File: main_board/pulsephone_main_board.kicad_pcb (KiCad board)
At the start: 2 copper layers, 70.5 x 128.5 mm, 32 parts, among them J1 USB_C_Receptacle_USB2.0_14P, J3 Conn_2Rows-35Pins_MountingPin, J4 Conn_2Rows-35Pins_MountingPin, J5 Conn_2Rows-35Pins_MountingPin, U1 XL1509-3.3, U2 PCM5102APWR, U4 TPS61202DRC, U5 TP4056-42-ESOP8

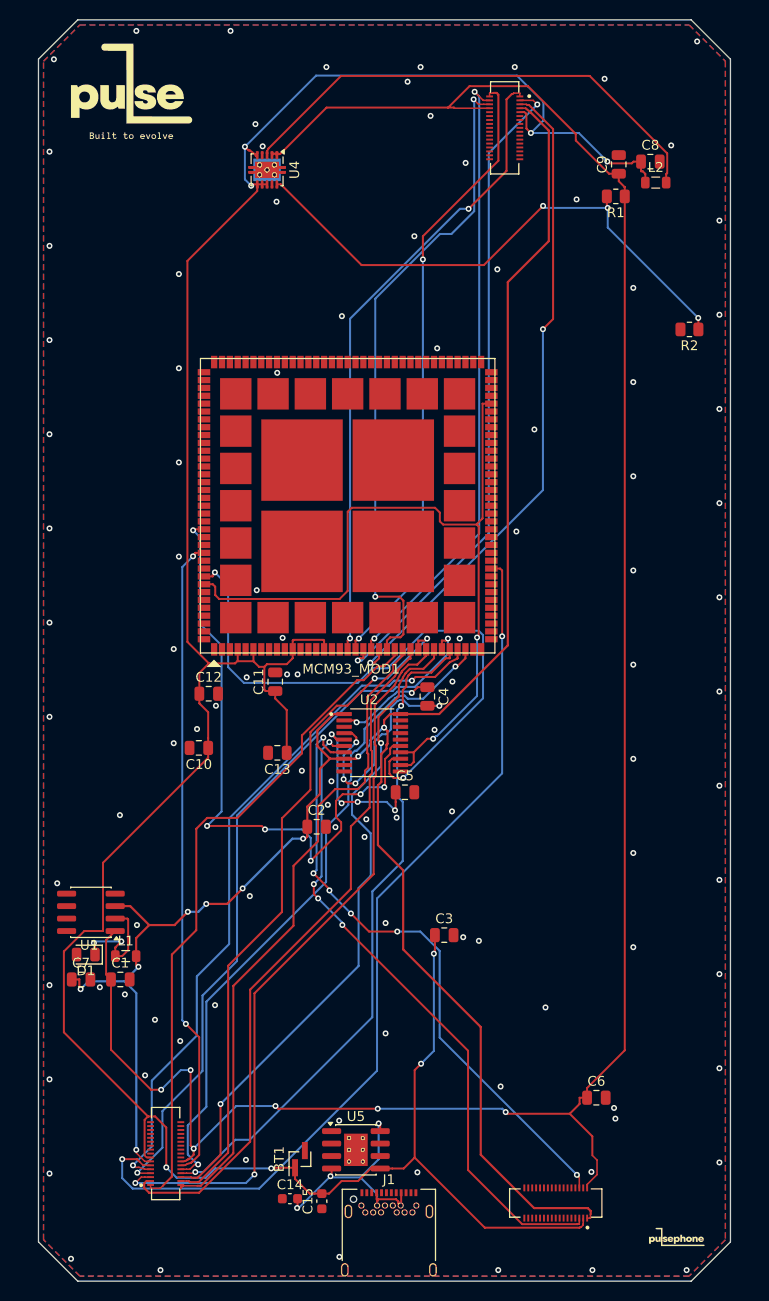
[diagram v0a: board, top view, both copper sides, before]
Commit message: pcb: update board layout and routing
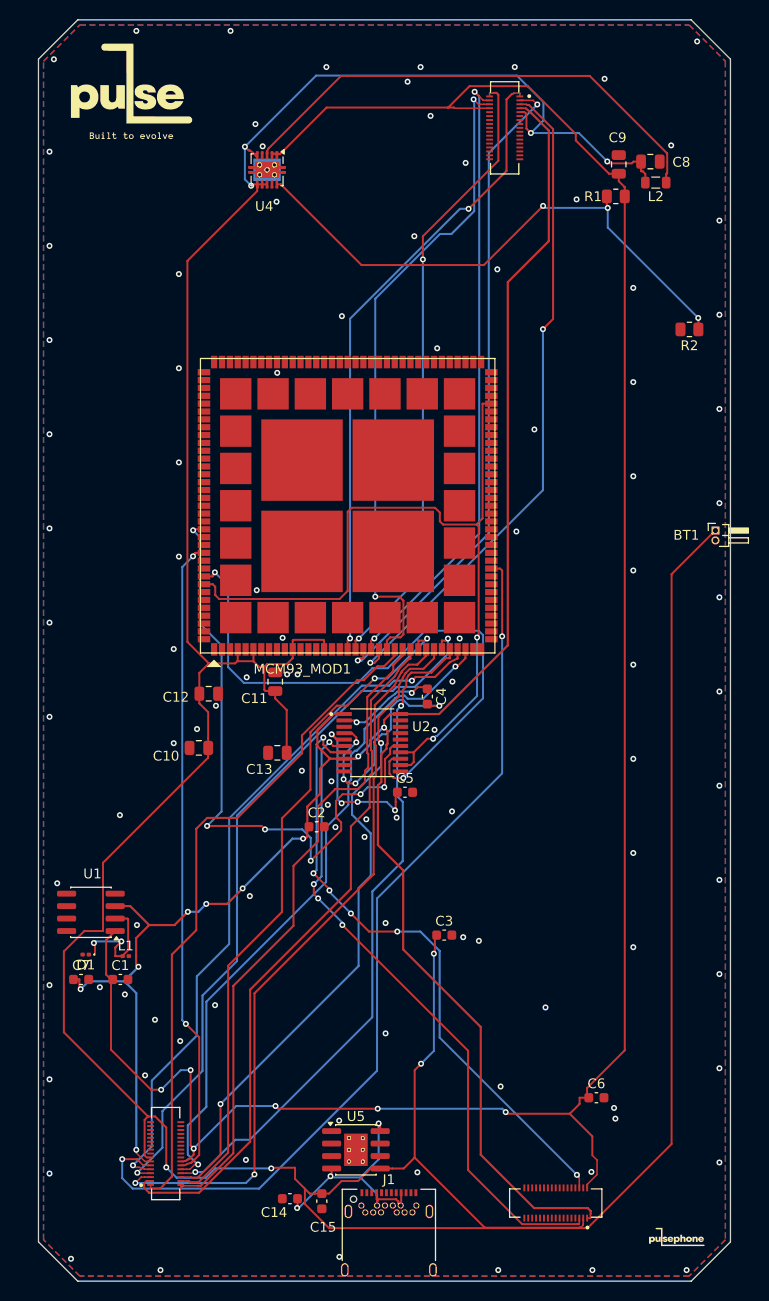
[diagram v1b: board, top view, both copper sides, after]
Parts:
- BT1: footprint Connector_PinHeader_1.00mm:PinHeader_1x02_P1.00mm_Vertical_SMD_Pin1Left -> Connector_PinHeader_1.00mm:PinHeader_1x02_P1.00mm_Horizontal
- C1, C4, C5, C7: footprint Capacitor_SMD:C_0805_2012Metric -> Capacitor_SMD:C_0603_1608Metric
- C2, C3, C6: value 20uF -> 10uF; footprint Capacitor_SMD:C_0805_2012Metric -> Capacitor_SMD:C_0603_1608Metric
- D1: footprint Diode_SMD:D_0805_2012Metric -> Diode_SMD:D_0201_0603Metric
- L1: footprint Inductor_SMD:L_0805_2012Metric -> Inductor_SMD:L_0201_0603Metric
- moved BT1 76.8 mm to (170.0, 78.0), turned to 0 degrees
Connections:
- C1 pad 1: +5V -> +3.7VBAT
- J5 pad 5: Net-(J5-Pin_5) -> unconnected-(J5-Pin_5-Pad5)
- J5 pad 6: Net-(J5-Pin_6) -> unconnected-(J5-Pin_6-Pad6)
- J5 pad 8: unconnected-(J5-Pin_8-Pad8) -> Net-(J5-Pin_8)
- J5 pad 9: unconnected-(J5-Pin_9-Pad9) -> Net-(J5-Pin_9)
- MCM93_MOD1 pad 11: +3.7VBAT -> +5V
- MCM93_MOD1 pad 133: /AUDIO_DATA_OUT -> /SAI_MASTERCLOCK
- MCM93_MOD1 pad 15: +3.7VBAT -> +5V
- MCM93_MOD1 pad 4: +3.7VBAT -> +5V
- MCM93_MOD1 pad 6: +3.7VBAT -> +5V
- U1 pad 1: +5V -> +3.7VBAT
- U1 pad 4: unconnected-(U1-~{EN}-Pad4) -> +3.7VBAT
- U2 pad 12: /AUDIO_DATA_OUT -> /SAI_MASTERCLOCK
- U2 pad 6: Net-(J5-Pin_5) -> Net-(J5-Pin_8)
- U2 pad 7: Net-(J5-Pin_6) -> Net-(J5-Pin_9)
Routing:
- net (no net): track 0.00 -> 130.4 mm, vias 0 -> 10
- net +3.7VBAT: track 287.0 -> 394.8 mm
- net Net-(J5-Pin_5): track 66.7 -> 0.00 mm, vias 4 -> 0
- net Net-(J5-Pin_6): track 63.8 -> 0.00 mm, vias 6 -> 0

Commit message: Redo PCB Routing, and added extra features
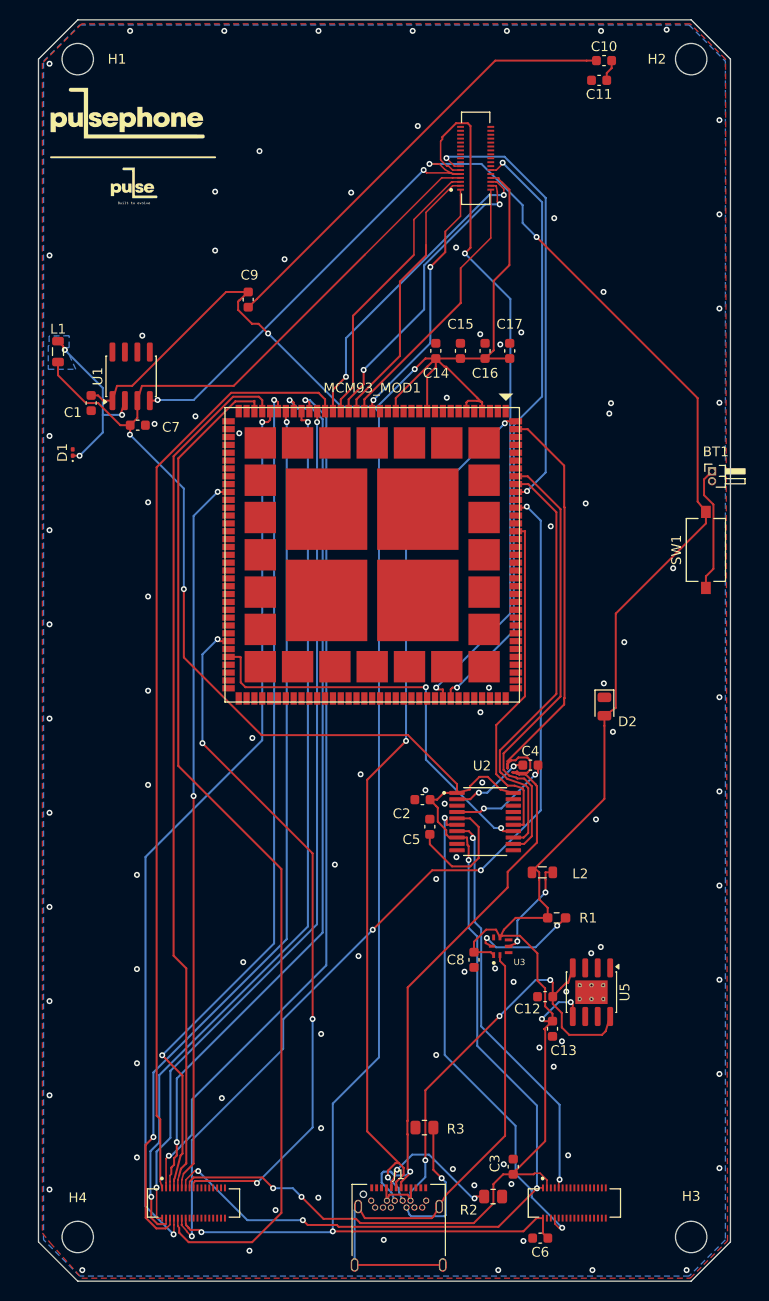
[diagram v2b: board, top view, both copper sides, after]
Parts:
- removed the G*** at (166.0, 150.0)
- removed U4: TPS61202DRC, Package_SON:Texas_S-PVSON-N10_ThermalVias
- removed nul: nul, LOGO
- added C16: 22uF, Capacitor_SMD:C_0603_1608Metric, F.Cu at (146.5, 59.7)
- added C17: 22uF, Capacitor_SMD:C_0603_1608Metric, F.Cu at (149.0, 59.7)
- added D2: LED, LED_SMD:LED_0805_2012Metric, F.Cu at (158.7, 96.0)
- added G***: LOGO, LOGO, F.Cu at (110.8, 43.0)
- added G***: LOGO, LOGO, F.Cu at (110.0, 35.5)
- added H1: MountingHole, MountingHole:MountingHole_3.2mm_M3, F.Cu at (105.0, 30.0)
- added H2: MountingHole, MountingHole:MountingHole_3.2mm_M3, F.Cu at (167.5, 30.0)
- added H3: MountingHole, MountingHole:MountingHole_3.2mm_M3, F.Cu at (167.5, 150.0)
- added H4: MountingHole, MountingHole:MountingHole_3.2mm_M3, F.Cu at (105.0, 150.0)
- added R3: 5.1 kΩ, Resistor_SMD:R_0805_2012Metric, F.Cu at (140.3, 138.9)
- added SW1: SW_DPST_x2, Button_Switch_SMD:SW_Tactile_SPST_NO_Straight_CK_PTS636Sx25SMTRLFS, F.Cu at (169.0, 80.0)
- added U3: ~, MIC2877-5.0YFT-TR:VREG_MIC2877-AYFT-TR, F.Cu at (148.1, 120.4)
- C10, C11, C8, C9: value 20uF -> 22uF; footprint Capacitor_SMD:C_0805_2012Metric -> Capacitor_SMD:C_0603_1608Metric
- C12, C13: value 20uF -> 10uF; footprint Capacitor_SMD:C_0805_2012Metric -> Capacitor_SMD:C_0603_1608Metric
- C14, C15: value 10uF -> 22uF
- L1: footprint Inductor_SMD:L_0201_0603Metric -> Inductor_SMD:L_0805_2012Metric
- L2: value 2.2uh -> 1uH
- R1: value 9Kohm -> 1Mega Ohm; footprint Resistor_SMD:R_0805_2012Metric -> Resistor_SMD:R_0603_1608Metric_Pad0.98x0.95mm_HandSolder
- R2: value 1Kohm -> 5.1 kΩ
- moved R2 90.6 mm to (147.3, 145.9), turned to 0 degrees
- moved C15 87.8 mm to (144.0, 59.7)
- moved C14 87.6 mm to (141.5, 59.7), turned to 90 degrees
- moved C8 83.3 mm to (145.4, 121.8), turned to -90 degrees
- moved C10 81.3 mm to (158.6, 30.1), turned to 0 degrees
- moved R1 73.8 mm to (153.8, 117.5)
- moved L2 71.2 mm to (152.3, 112.9)
- moved C11 69.6 mm to (158.1, 32.2), turned to 180 degrees
- moved L1 62.0 mm to (103.0, 59.8), turned to -90 degrees
- moved C1 58.8 mm to (106.4, 65.0), turned to -90 degrees
- moved C7 56.8 mm to (111.1, 67.3)
- moved U1 54.8 mm to (110.4, 62.3), turned to 90 degrees
- moved D1 51.2 mm to (104.5, 70.1), turned to 90 degrees
- moved C12 46.1 mm to (152.6, 125.5)
- moved C9 40.2 mm to (122.4, 54.5), turned to -90 degrees
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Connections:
- BT1 pad 1: +3.7VBAT -> Net-(BT1-+)
- C1 pad 1: +3.7VBAT -> +5V
- C10 pad 1: +3.7VBAT -> Net-(C10-Pad1)
- C10 pad 2: GND -> Net-(C10-Pad2)
- C11 pad 1: +3.7VBAT -> Net-(C10-Pad2)
- C12 pad 1: +3.7VBAT -> GND
- C12 pad 2: GND -> Net-(U5-CE)
- C13 pad 1: +3.7VBAT -> GND
- C13 pad 2: GND -> +3.7VBAT
- C14 pad 1: GND -> +5V
- C14 pad 2: Net-(U5-CE) -> GND
- C15 pad 1: GND -> +5V
- C15 pad 2: +3.7VBAT -> GND
- C9 pad 2: GND -> Net-(C10-Pad1)
- J1 pad A5: unconnected-(J1-CC1-PadA5) -> Net-(J1-CC1)
- J1 pad A6: unconnected-(J1-D+-PadA6) -> USB_DP
- J1 pad A7: unconnected-(J1-D--PadA7) -> USB_DN
- J1 pad B5: unconnected-(J1-CC2-PadB5) -> Net-(J1-CC2)
- J1 pad B6: unconnected-(J1-D+-PadB6) -> USB_DP
- J1 pad B7: unconnected-(J1-D--PadB7) -> USB_DN
- J1 pad S1: unconnected-(J1-SHIELD-PadS1) -> GNDCHASSIS
- J3 pad 11: unconnected-(J3-Pin_11-Pad11) -> CAM_I2C_SCL
- J3 pad 12: unconnected-(J3-Pin_12-Pad12) -> CAM_I2C_SDA
- J3 pad 13: unconnected-(J3-Pin_13-Pad13) -> CAM_GPIO
- J4 pad 17: unconnected-(J4-Pin_17-Pad17) -> RST
- MCM93_MOD1 pad 131: unconnected-(MCM93_MOD1D-26-Pad131) -> CAM_GPIO
- MCM93_MOD1 pad 139: unconnected-(MCM93_MOD1D-34-Pad139) -> USB_DN
- MCM93_MOD1 pad 140: unconnected-(MCM93_MOD1D-35-Pad140) -> USB_DP
- MCM93_MOD1 pad 64: unconnected-(MCM93_MOD1B-29-Pad64) -> RST
- MCM93_MOD1 pad 97: unconnected-(MCM93_MOD1C-27-Pad97) -> CAM_I2C_SCL
- MCM93_MOD1 pad 98: unconnected-(MCM93_MOD1C-28-Pad98) -> CAM_I2C_SDA
- R1 pad 1: +5V -> Power Good
- R1 pad 2: Net-(U4-FB) -> +3.7VBAT
- R2 pad 1: Net-(U4-FB) -> Net-(J1-CC1)
- U1 pad 1: +3.7VBAT -> +5V
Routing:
- net +3.7VBAT: track 394.8 -> 236.6 mm
- net (no net): track 130.4 -> 0.00 mm, vias 10 -> 0
- net USB_DN: track 0.00 -> 102.4 mm, vias 0 -> 1
- net USB_DP: track 0.00 -> 91.8 mm, vias 0 -> 3
- net CAM_I2C_SCL: track 0.00 -> 72.6 mm, vias 0 -> 2
- net RST: track 0.00 -> 71.4 mm, vias 0 -> 4
- net CAM_I2C_SDA: track 0.00 -> 62.0 mm, vias 0 -> 2
- net Net-(U4-FB): track 57.1 -> 0.00 mm, vias 3 -> 0
- net GNDCHASSIS: track 0.00 -> 53.2 mm
- net Net-(J5-Pin_8): track 0.00 -> 50.1 mm, vias 0 -> 2
- net Net-(C10-Pad1): track 0.00 -> 45.9 mm
- net /SAI_MASTERCLOCK: track 0.00 -> 45.7 mm
- net CAM_GPIO: track 0.00 -> 45.5 mm, vias 0 -> 2
- net Net-(J5-Pin_9): track 0.00 -> 41.4 mm, vias 0 -> 2
- net Net-(U3-SW): track 50.7 -> 10.0 mm, vias 0 -> 2
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
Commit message: add extra ground pins to high speed MIPI LANES for reduction of signal coupling.
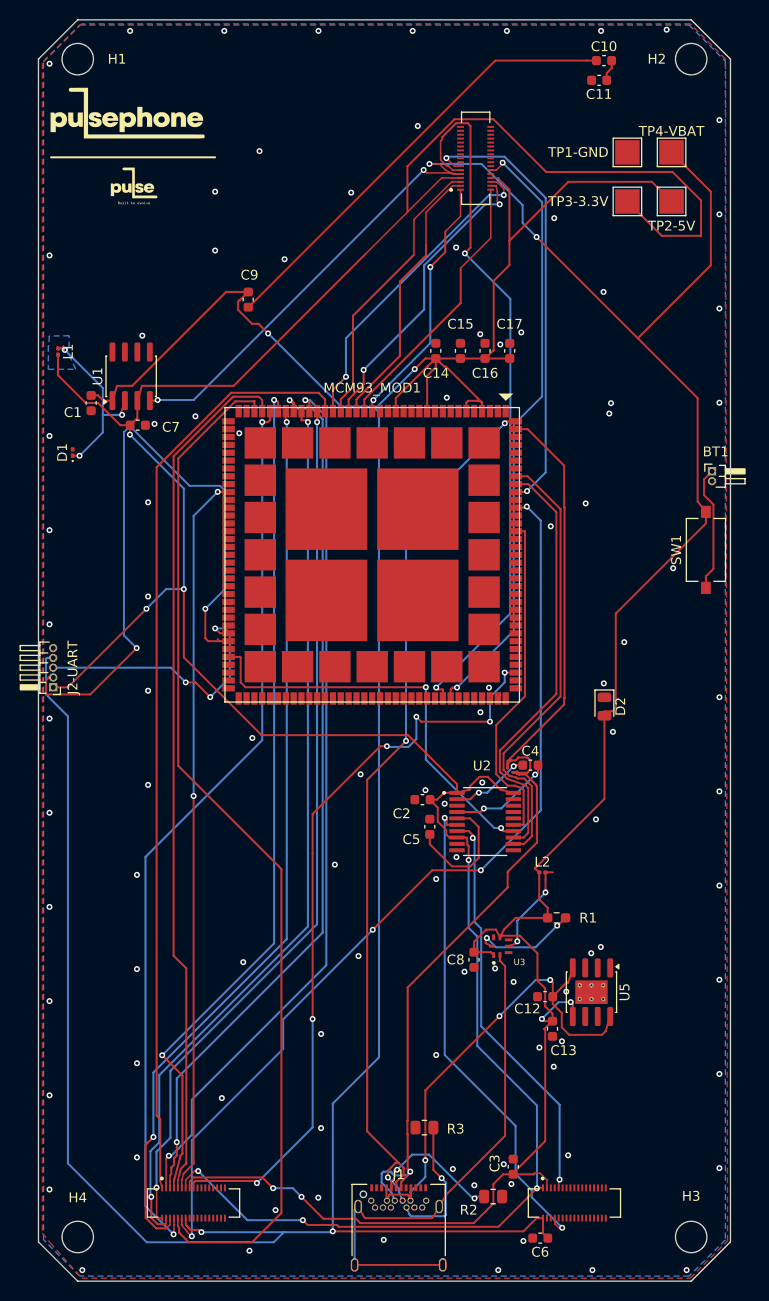
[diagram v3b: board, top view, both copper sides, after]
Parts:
- added J2-UART: Conn_01x05, Connector_PinHeader_1.00mm:PinHeader_1x05_P1.00mm_Horizontal, F.Cu at (102.5, 94.0)
- added TP1-GND: TestPoint, TestPoint:TestPoint_Pad_2.5x2.5mm, F.Cu at (161.0, 39.5)
- added TP2-5V: TestPoint, TestPoint:TestPoint_Pad_2.5x2.5mm, F.Cu at (165.5, 44.5)
- added TP3-3.3V: TestPoint, TestPoint:TestPoint_Pad_2.5x2.5mm, F.Cu at (161.0, 44.5)
- added TP4-VBAT: TestPoint, TestPoint:TestPoint_Pad_2.5x2.5mm, F.Cu at (165.5, 39.5)
- L1, L2: footprint Inductor_SMD:L_0805_2012Metric -> Inductor_SMD:L_0201_0603Metric
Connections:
- MCM93_MOD1 pad 108: unconnected-(MCM93_MOD1D-3-Pad108) -> RST
- MCM93_MOD1 pad 63: unconnected-(MCM93_MOD1B-28-Pad63) -> UART_TX
- MCM93_MOD1 pad 64: RST -> UART_RX
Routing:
- net +5V: track 227.3 -> 326.0 mm
- net +3.3V: track 213.3 -> 284.0 mm, vias 6 -> 7
- net UART_RX: track 0.00 -> 67.6 mm, vias 0 -> 2
- net UART_TX: track 0.00 -> 28.4 mm, vias 0 -> 3
- net +3.7VBAT: track 236.6 -> 260.6 mm
- net RST: track 71.4 -> 77.7 mm, vias 4 -> 6

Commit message: rewire traces for new connector scheme
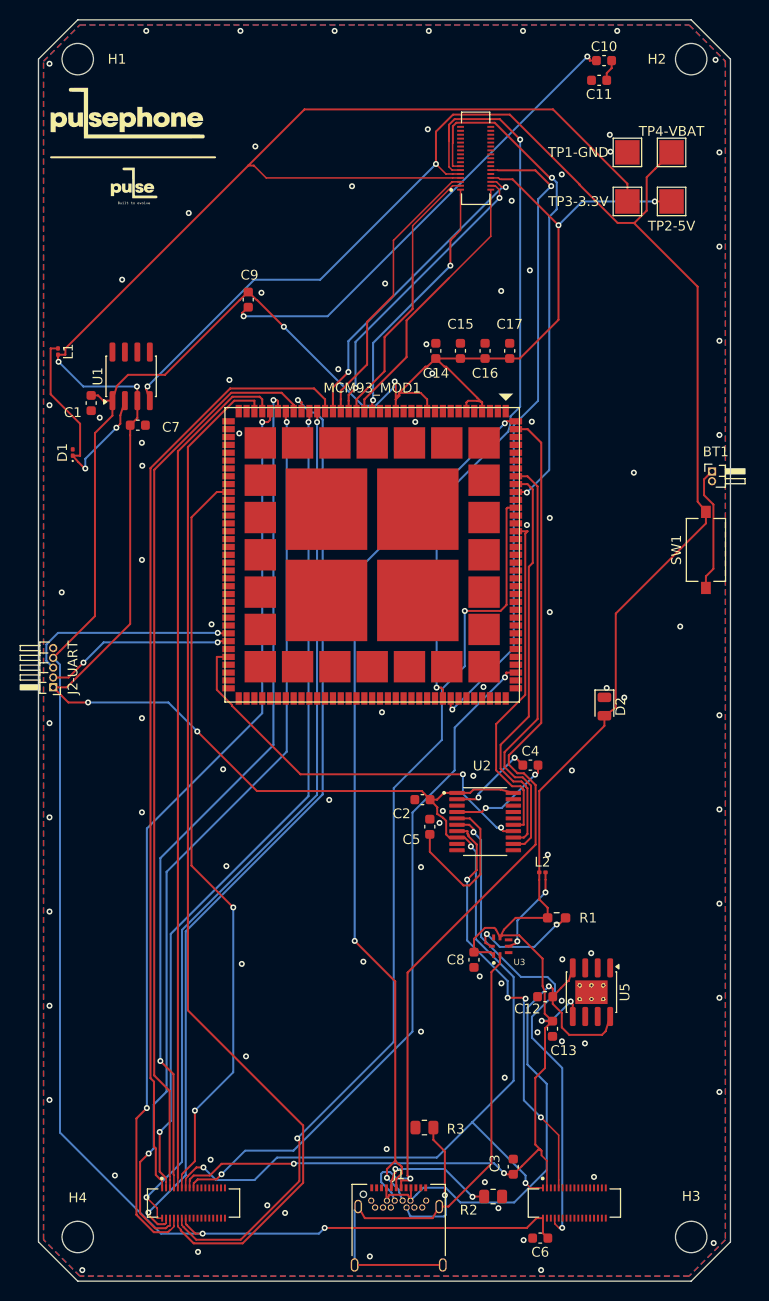
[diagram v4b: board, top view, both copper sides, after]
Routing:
- net +5V: track 326.0 -> 248.1 mm, vias 4 -> 6
- net UART_RX: track 67.6 -> 19.4 mm
- net +3.7VBAT: track 260.6 -> 250.8 mm, vias 8 -> 6
- net +3.3V: track 284.0 -> 275.9 mm
- net USB_DN: track 102.4 -> 94.9 mm
- net Net-(U5-CE): track 50.7 -> 57.7 mm, vias 3 -> 1
- net RST: track 77.7 -> 70.7 mm, vias 6 -> 2
- net UART_TX: track 28.4 -> 21.7 mm, vias 3 -> 1
- net CAM_GPIO: track 45.5 -> 52.1 mm
- net Net-(D1-K): track 18.6 -> 24.0 mm, vias 3 -> 2
- net /DSI_D0_P: track 91.8 -> 95.8 mm
- net /DSI_D0_N: track 89.7 -> 85.7 mm
- net /I2C3_SCL: track 73.5 -> 77.1 mm
- net CAM_I2C_SDA: track 62.0 -> 65.5 mm
- net Net-(U2-VNEG): track 13.0 -> 16.3 mm
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
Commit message: test
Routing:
- added copper zone on In1.Cu, net GND
- added copper zone on In2.Cu, net GND
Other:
- copper layers 2 -> 4

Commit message: fix some errors
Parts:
- added R4: 1.2 kΩ, Resistor_SMD:R_0805_2012Metric, F.Cu at (159.6, 119.2)
- renumbered J2-UART to J2, TP1-GND to TP1, TP2-5V to TP2, TP3-3.3V to TP3, TP4-VBAT to TP4
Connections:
- J3 pad 10: GND -> /CSI_D1_P
- J3 pad 11: CAM_I2C_SCL -> GND
- J3 pad 12: CAM_I2C_SDA -> GND
- J3 pad 13: CAM_GPIO -> +3.3V
- J3 pad 14: unconnected-(J3-Pin_14-Pad14) -> +5V
- J3 pad 15: unconnected-(J3-Pin_15-Pad15) -> +3.7VBAT
- J3 pad 16: unconnected-(J3-Pin_16-Pad16) -> GND
- J3 pad 17: unconnected-(J3-Pin_17-Pad17) -> CAM_I2C_SCL
- J3 pad 18: unconnected-(J3-Pin_18-Pad18) -> CAM_I2C_SDA
- J3 pad 19: unconnected-(J3-Pin_19-Pad19) -> CAM_GPIO
- J3 pad 3: /CSI_D0_N -> GND
- J3 pad 4: /CSI_D0_P -> GND
- J3 pad 5: /CSI_D1_N -> /CSI_D0_N
- J3 pad 6: /CSI_D1_P -> /CSI_D0_P
- J3 pad 7: +3.3V -> GND
- J3 pad 8: +5V -> GND
- J3 pad 9: +3.7VBAT -> /CSI_D1_N
- J4 pad 10: /DSI_D3_P -> /DSI_D1_P
- J4 pad 11: /I2C3_SCL -> GND
- J4 pad 12: /I2C3_SDA -> GND
- J4 pad 13: +3.3V -> /DSI_D2_N
- J4 pad 14: +5V -> /DSI_D2_P
- J4 pad 15: +3.7VBAT -> GND
- J4 pad 17: RST -> /DSI_D3_N
- J4 pad 18: unconnected-(J4-Pin_18-Pad18) -> /DSI_D3_P
- J4 pad 19: unconnected-(J4-Pin_19-Pad19) -> GND
- J4 pad 20: unconnected-(J4-Pin_20-Pad20) -> GND
- J4 pad 21: unconnected-(J4-Pin_21-Pad21) -> /I2C3_SCL
- J4 pad 22: unconnected-(J4-Pin_22-Pad22) -> /I2C3_SDA
- J4 pad 23: unconnected-(J4-Pin_23-Pad23) -> +3.3V
- J4 pad 24: unconnected-(J4-Pin_24-Pad24) -> +5V
- J4 pad 25: unconnected-(J4-Pin_25-Pad25) -> +3.7VBAT
- J4 pad 26: unconnected-(J4-Pin_26-Pad26) -> GND
- J4 pad 27: unconnected-(J4-Pin_27-Pad27) -> RST
- J4 pad 3: /DSI_D0_N -> GND
- J4 pad 4: /DSI_D0_P -> GND
- J4 pad 5: /DSI_D1_N -> /DSI_D0_N
- J4 pad 6: /DSI_D1_P -> /DSI_D0_P
- J4 pad 7: /DSI_D2_N -> GND
- J4 pad 8: /DSI_D2_P -> GND
- J4 pad 9: /DSI_D3_N -> /DSI_D1_N
- U5 pad 2: unconnected-(U5-PROG-Pad2) -> Net-(U5-PROG)
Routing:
- net Net-(U5-PROG): track 0.00 -> 3.63 mm
